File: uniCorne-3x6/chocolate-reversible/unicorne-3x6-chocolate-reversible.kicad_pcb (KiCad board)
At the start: 2 copper layers, 133.8 x 91.4 mm, 98 parts, among them J1 MJ-4PP-9, J2 Conn_01x05, J3 Conn_01x02, J4 Conn_01x03, SW1 SW_CHOC_HS, SW10 SW_CHOC_HS, SW11 SW_CHOC_HS, SW12 SW_CHOC_HS, SW13 SW_CHOC_HS, SW14 SW_CHOC_HS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

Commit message: fixed 3x6
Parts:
- added JP10: , TB2086_MISC:SolderJumper-2_P1.3mm_Open_TrianglePad1.0x1.2mm_rev, F.Cu at (181.6, 114.0)
- added JP11: , TB2086_MISC:SolderJumper-2_P1.3mm_Open_TrianglePad1.0x1.2mm_rev, F.Cu at (173.0, 82.6)
- moved R3 0.70 mm to (184.3, 110.5)
- moved R4 0.68 mm to (184.4, 112.4)
- moved JP9 0.36 mm to (188.2, 111.1)
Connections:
- J1 pad A: SCL -> Net-(JP10-B)
- U1 pad 24: unconnected-(U1-RAW-Pad24) -> BAT+
- U1 pad 26: GND -> B-/D-
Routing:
- net B-/D-: track 0.00 -> 31.9 mm, vias 0 -> 3
- net GND: track 45.8 -> 22.7 mm, vias 26 -> 23
- net unconnected-(U1-RAW-Pad24): track 11.0 -> 0.00 mm, vias 1 -> 0
- net Net-(JP10-B): track 0.00 -> 6.89 mm
- net BAT+: track 14.0 -> 19.6 mm
- net SCL: track 58.5 -> 54.8 mm, vias 4 -> 5
- net row0: track 167.8 -> 170.4 mm
- net Net-(L12-DOUT): track 44.9 -> 46.6 mm
- net VCC: track 589.9 -> 591.3 mm
- net Net-(D6-A): track 11.8 -> 11.0 mm
- net SDA: track 68.2 -> 69.0 mm

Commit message: Docs / KiCad8 (#12)
* KiCAD 8

* KiCad8 for plates

* Update Footprints

* Update README.md

* added more docs
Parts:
- D1, D10, D11, D12, D13, D14, D15, D16, D17, D18, D19, D2, D20, D21, D3, D4, D5, D6, D7, D8, D9: moved to F.Cu
- JP10, JP11: value (none) -> ~

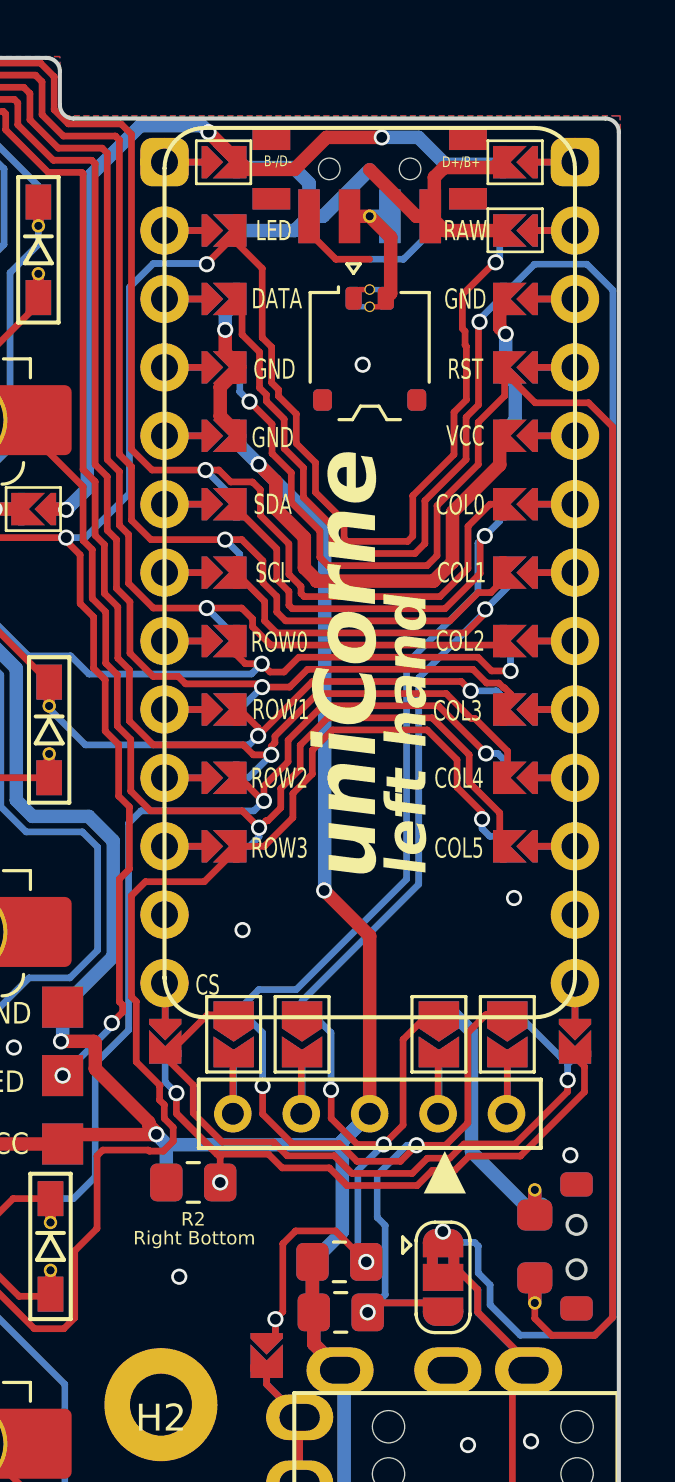
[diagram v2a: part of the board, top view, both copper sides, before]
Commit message: fixed SDA/SCL shorted
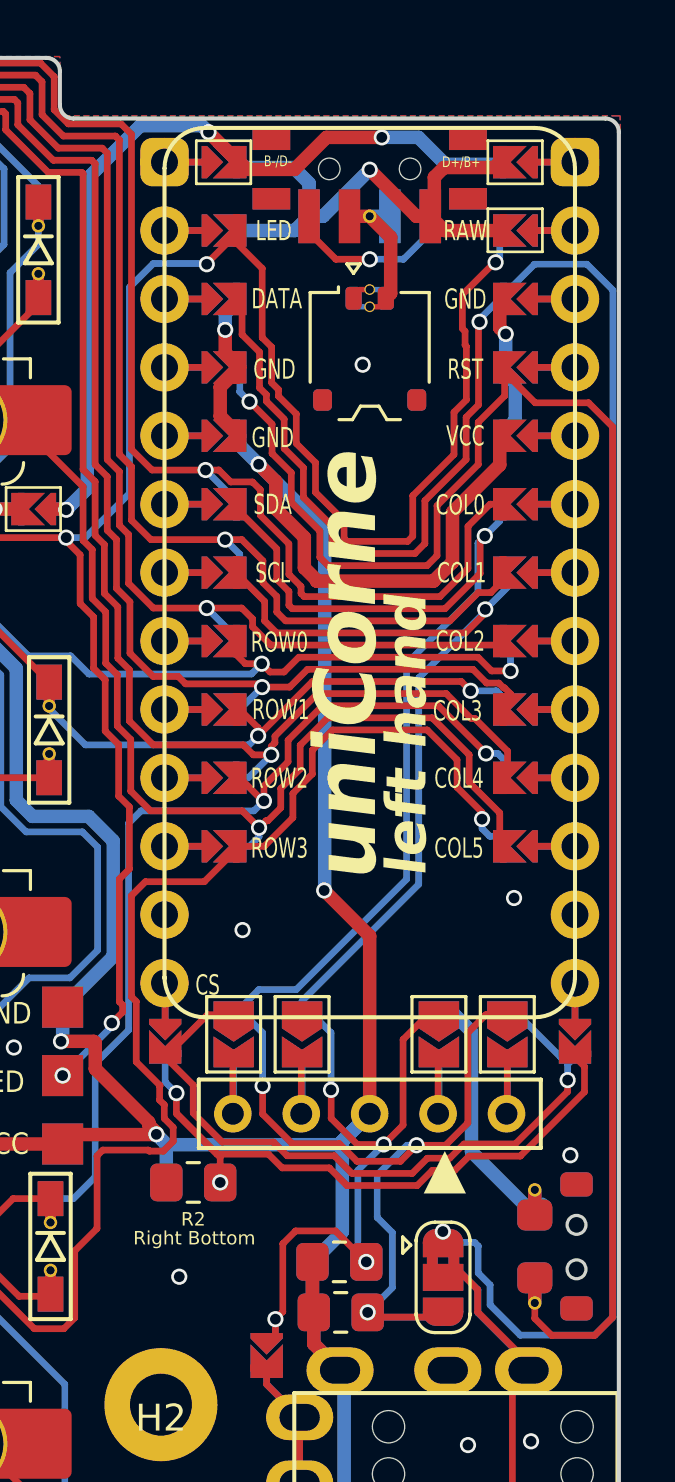
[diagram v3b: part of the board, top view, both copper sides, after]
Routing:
- net unconnected-(PSW1-C-Pad3)_1: track 5.32 -> 5.92 mm, vias 0 -> 1
- net SDA: track 69.0 -> 69.5 mm
- net BAT+: vias 0 -> 1
